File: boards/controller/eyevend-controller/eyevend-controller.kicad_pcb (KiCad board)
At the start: 4 copper layers, 63.5 x 76.2 mm, 22 parts, among them J1 Barrel_Jack_Switch, J2 sig, J3 swd, J4 pwr_utilL, J5 Conn_01x15, J6 Micro_SD_Card_Det1, J7 Conn_01x15, J8 pwr_utilR, J9 sig, SW1 SW_Push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

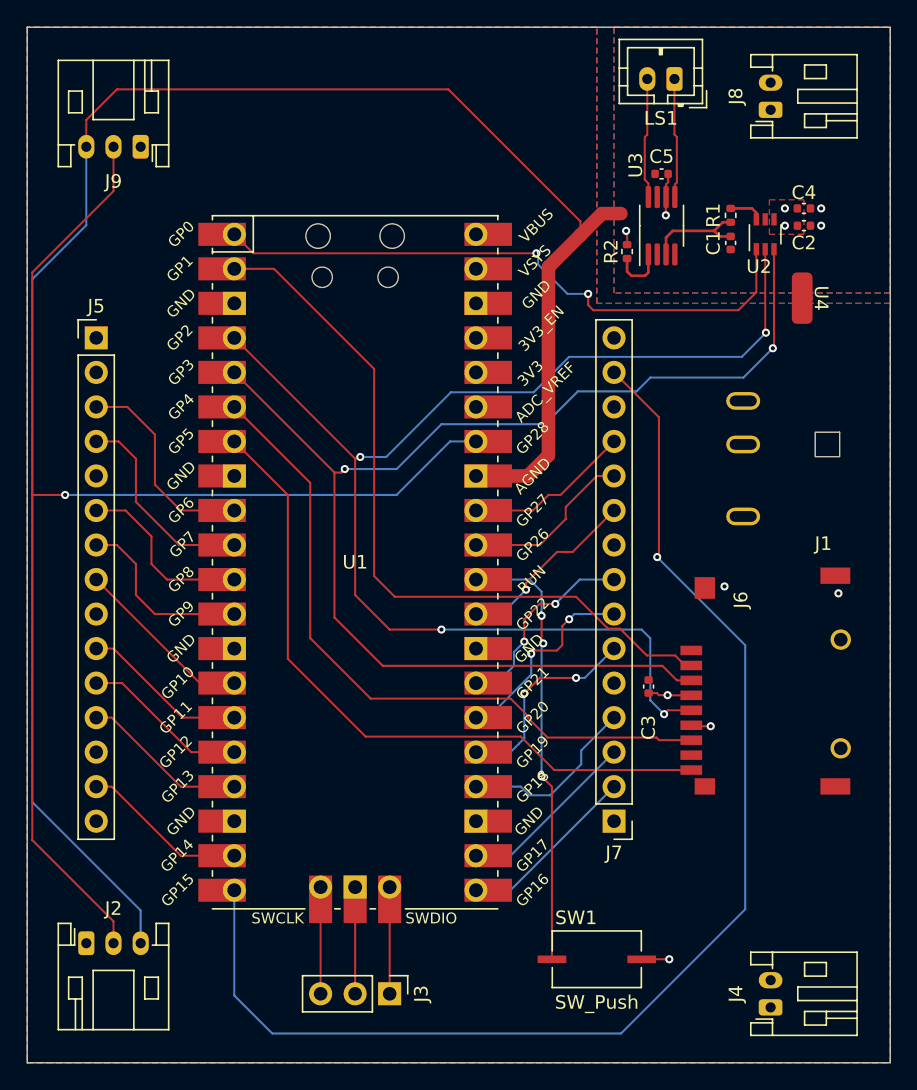
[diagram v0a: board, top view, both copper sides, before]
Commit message: added mounting holes
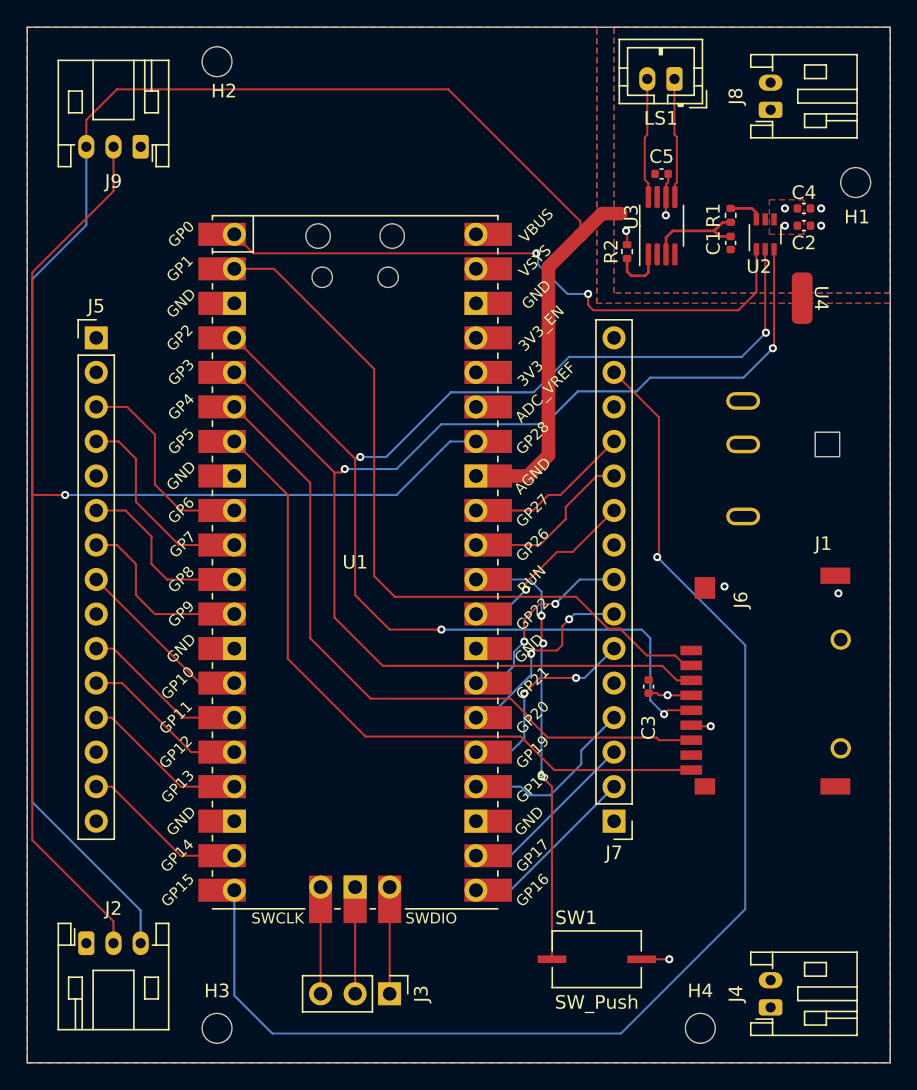
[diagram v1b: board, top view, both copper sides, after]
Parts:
- added H1: MountingHole_Pad, MountingHole:MountingHole_2.2mm_M2_ISO7380, F.Cu at (200.7, 49.5)
- added H2: MountingHole_Pad, MountingHole:MountingHole_2.2mm_M2_ISO7380, F.Cu at (153.7, 40.6)
- added H3: MountingHole_Pad, MountingHole:MountingHole_2.2mm_M2_ISO7380, F.Cu at (153.7, 111.8)
- added H4: MountingHole_Pad, MountingHole:MountingHole_2.2mm_M2_ISO7380, F.Cu at (189.2, 111.8)
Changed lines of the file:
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@@
     )
+  )
+  (footprint "MountingHole:MountingHole_2.2mm_M2_ISO7380" (layer "F.Cu")
+    (at 153.67 40.64)
+    (descr "Mounting Hole 2.2mm, no annular, M2, ISO7380")
+    (tags "mounting hole 2.2mm no annular m2 iso7380")
+    (property "Sheetfile" "eyevend-controller.kicad_sch")
+    (property "Sheetname" "")
+    (property "ki_description" "Mounting Hole with connection")
+    (property "ki_keywords" "mounting hole")
+    (attr exclude_from_pos_files)
+    (fp_text reference "H2" (at 0.51 2.16) (layer "F.SilkS")
+        (effects (font (size 1 1) (thickness 0.15)))
+    )
+    (fp_text value "MountingHole_Pad" (at 0 2.75) (layer "F.Fab")
+        (effects (font (size 1 1) (thickness 0.15)))
+    )
+    (fp_text user "${REFERENCE}" (at 0 0) (layer "F.Fab")
+        (effects (font (size 1 1) (thickness 0.15)))
+    )
+    (fp_circle (center 0 0) (end 1.75 0)
+      (stroke (width 0.15) (type solid)) (fill none) (layer "Cmts.User"))
+    (fp_circle (center 0 0) (end 2 0)
+      (stroke (width 0.05) (type solid)) (fill none) (layer "F.CrtYd"))
+    (pad "" np_thru_hole circle (at 0 0) (size 2.2 2.2) (drill 2.2) (layers "*.Cu" "*.Mask"))
   )
   (footprint "Connector_PinHeader_2.54mm:PinHeader_1x15_P2.54mm_Vertical" (layer "F.Cu")
@@
       (rotate (xyz 0 0 0))
     )
+  )
+  (footprint "MountingHole:MountingHole_2.2mm_M2_ISO7380" (layer "F.Cu")
+    (at 200.66 49.53)
+    (descr "Mounting Hole 2.2mm, no annular, M2, ISO7380")
+    (tags "mounting hole 2.2mm no annular m2 iso7380")
+    (property "Sheetfile" "eyevend-controller.kicad_sch")
+    (property "Sheetname" "")
+    (property "ki_description" "Mounting Hole with connection")
+    (property "ki_keywords" "mounting hole")
+    (attr exclude_from_pos_files)
+    (fp_text reference "H1" (at 0.1 2.54) (layer "F.SilkS")
+        (effects (font (size 1 1) (thickness 0.15)))
+    )
+    (fp_text value "MountingHole_Pad" (at 0 2.75) (layer "F.Fab")
+        (effects (font (size 1 1) (thickness 0.15)))
+    )
+    (fp_text user "${REFERENCE}" (at 0 0) (layer "F.Fab")
+        (effects (font (size 1 1) (thickness 0.15)))
+    )
+    (fp_circle (center 0 0) (end 1.75 0)
+      (stroke (width 0.15) (type solid)) (fill none) (layer "Cmts.User"))
+    (fp_circle (center 0 0) (end 2 0)
+      (stroke (width 0.05) (type solid)) (fill none) (layer "F.CrtYd"))
+    (pad "" np_thru_hole circle (at 0 0) (size 2.2 2.2) (drill 2.2) (layers "*.Cu" "*.Mask"))
   )
   (footprint "JFHsd:GT-TF003-H0185-02" (layer "F.Cu")
@@
     )
   )
+  (footprint "MountingHole:MountingHole_2.2mm_M2_ISO7380" (layer "F.Cu")
+    (at 153.67 111.76)
+    (descr "Mounting Hole 2.2mm, no annular, M2, ISO7380")
+    (tags "mounting hole 2.2mm no annular m2 iso7380")
+    (property "Sheetfile" "eyevend-controller.kicad_sch")
+    (property "Sheetname" "")
+    (property "ki_description" "Mounting Hole with connection")
+    (property "ki_keywords" "mounting hole")
+    (attr exclude_from_pos_files)
+    (fp_text reference "H3" (at 0 -2.75) (layer "F.SilkS")
+        (effects (font (size 1 1) (thickness 0.15)))
+    )
+    (fp_text value "MountingHole_Pad" (at 0 2.75) (layer "F.Fab")
+        (effects (font (size 1 1) (thickness 0.15)))
+    )
+    (fp_text user "${REFERENCE}" (at 0 0) (layer "F.Fab")
+        (effects (font (size 1 1) (thickness 0.15)))
+    )
+    (fp_circle (center 0 0) (end 1.75 0)
+      (stroke (width 0.15) (type solid)) (fill none) (layer "Cmts.User"))
+    (fp_circle (center 0 0) (end 2 0)
+      (stroke (width 0.05) (type solid)) (fill none) (layer "F.CrtYd"))
+    (pad "" np_thru_hole circle (at 0 0) (size 2.2 2.2) (drill 2.2) (layers "*.Cu" "*.Mask"))
+  )
   (footprint "Package_TO_SOT_SMD:Texas_R-PDSO-G6" (layer "F.Cu")
     (at 194 53.34 90)
@@
     (property "ki_keywords" "audio amplifier class d")
     (attr smd)
-    (fp_text reference "U3" (at 4.445 -1.905 90) (layer "F.SilkS")
+    (fp_text reference "U3" (at 0.635 -2.23 90) (layer "F.SilkS")
         (effects (font (size 1 1) (thickness 0.15)))
     )
@@
       (net 5 "GND") (pinfunction "2") (pintype "passive"))
   )
+  (footprint "MountingHole:MountingHole_2.2mm_M2_ISO7380" (layer "F.Cu")
+    (at 189.23 111.76)
+    (descr "Mounting Hole 2.2mm, no annular, M2, ISO7380")
+    (tags "mounting hole 2.2mm no annular m2 iso7380")
+    (property "Sheetfile" "eyevend-controller.kicad_sch")
+    (property "Sheetname" "")
+    (property "ki_description" "Mounting Hole with connection")
+    (property "ki_keywords" "mounting hole")
+    (attr exclude_from_pos_files)
+    (fp_text reference "H4" (at 0 -2.75) (layer "F.SilkS")
+        (effects (font (size 1 1) (thickness 0.15)))
+    )
+    (fp_text value "MountingHole_Pad" (at 0 2.75) (layer "F.Fab")
+        (effects (font (size 1 1) (thickness 0.15)))
+    )
+    (fp_text user "${REFERENCE}" (at 0 0) (layer "F.Fab")
+        (effects (font (size 1 1) (thickness 0.15)))
+    )
+    (fp_circle (center 0 0) (end 1.75 0)
+      (stroke (width 0.15) (type solid)) (fill none) (layer "Cmts.User"))
+    (fp_circle (center 0 0) (end 2 0)
+      (stroke (width 0.05) (type solid)) (fill none) (layer "F.CrtYd"))
+    (pad "" np_thru_hole circle (at 0 0) (size 2.2 2.2) (drill 2.2) (layers "*.Cu" "*.Mask"))
+  )
   (gr_rect (start 139.7 38.1) (end 203.2 114.3)
